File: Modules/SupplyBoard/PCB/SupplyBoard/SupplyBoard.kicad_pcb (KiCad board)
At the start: 2 copper layers, 20.3 x 8.4 mm, 4 parts, among them J1 CI_BATT, J2 USB_B_Mini, J3 Bus_PCI_Express_x1, U1 STM32L031G6Ux

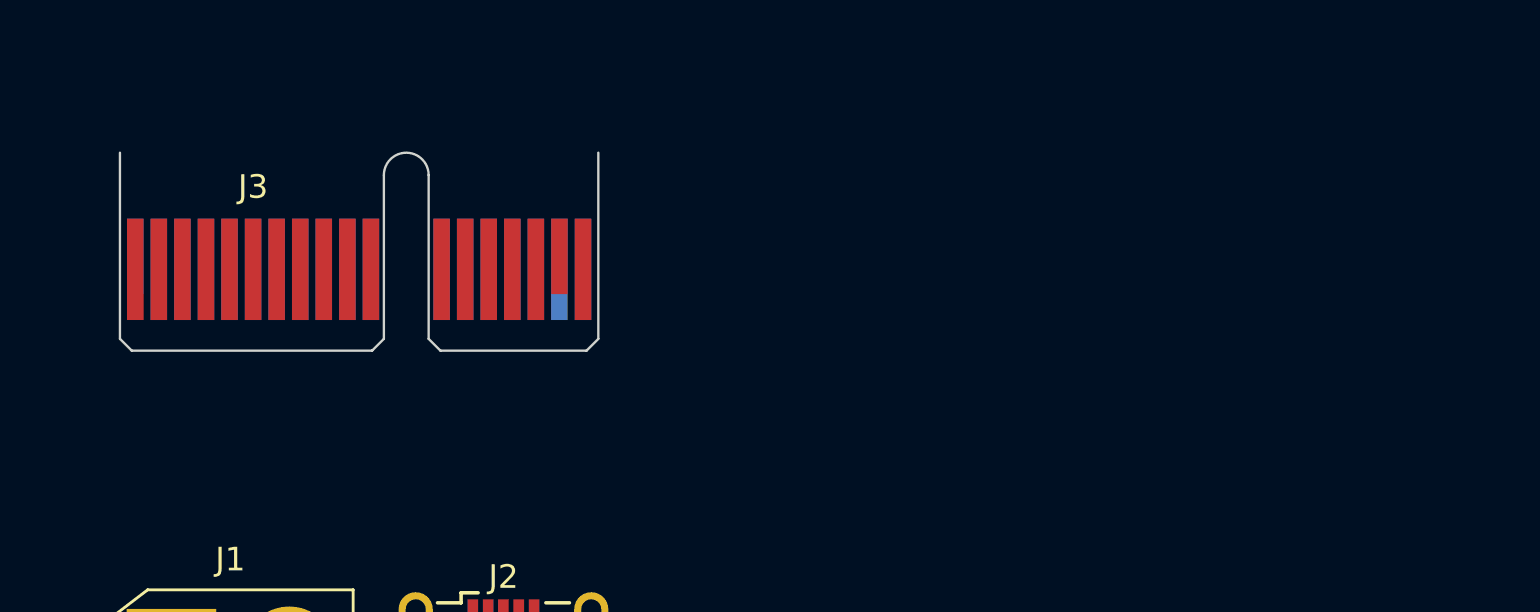
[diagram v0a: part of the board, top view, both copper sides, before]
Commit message: Lipo to 3v3 circuit added
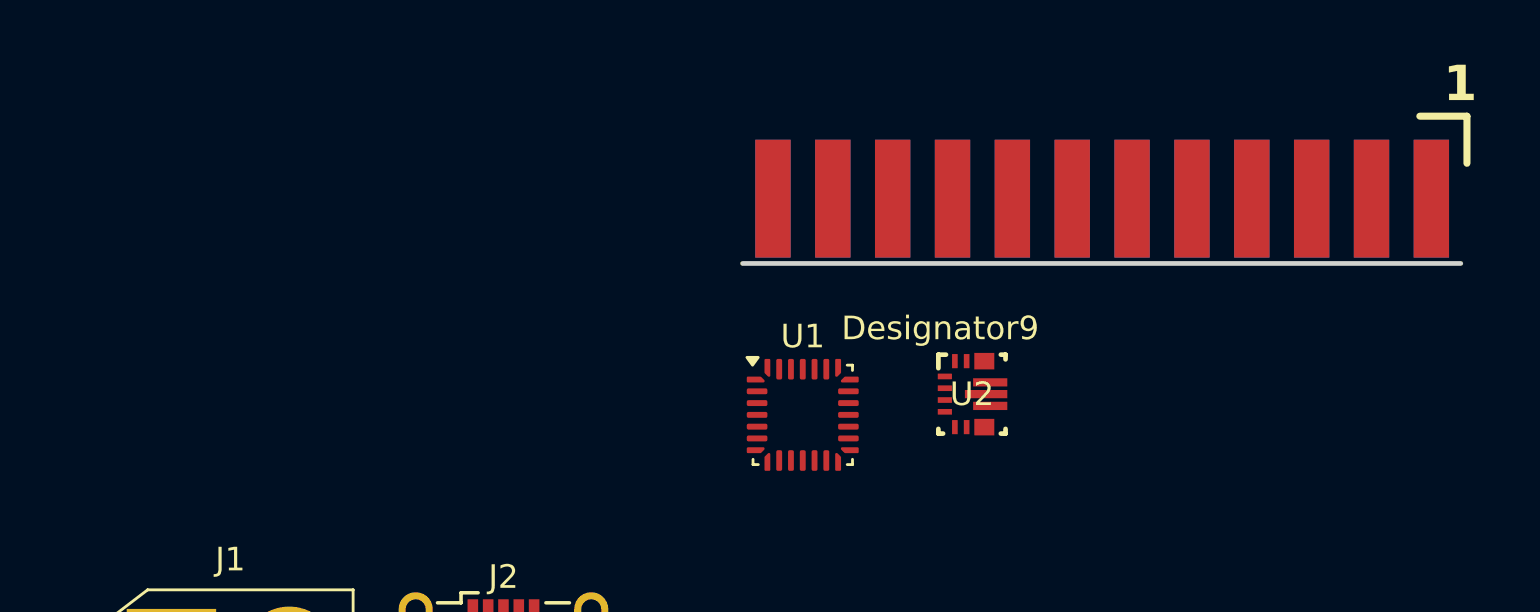
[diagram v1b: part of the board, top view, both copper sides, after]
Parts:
- added U1: STM32L031G6Ux, Package_DFN_QFN:QFN-28_4x4mm_P0.5mm, F.Cu at (104.3, 59.7)
- added U2: TPS63070, IcaroFootprints:RNM0015A, F.Cu at (111.5, 58.8)
- J3: value Bus_PCI_Express_x1 -> CIO_MAIN_CONNECTOR; footprint Connector_PCBEdge:BUS_PCIexpress_x1 -> IcaroFootprints:Connector_Icaro_Edge_tarjeta
- moved J3 41.1 mm to (117.0, 50.5)
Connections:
- J1 pad 1: unconnected-(J1-Pin_1-Pad1) -> GND
- J1 pad 2: unconnected-(J1-Pin_2-Pad2) -> /LIPO_INPUT
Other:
- board outline removed

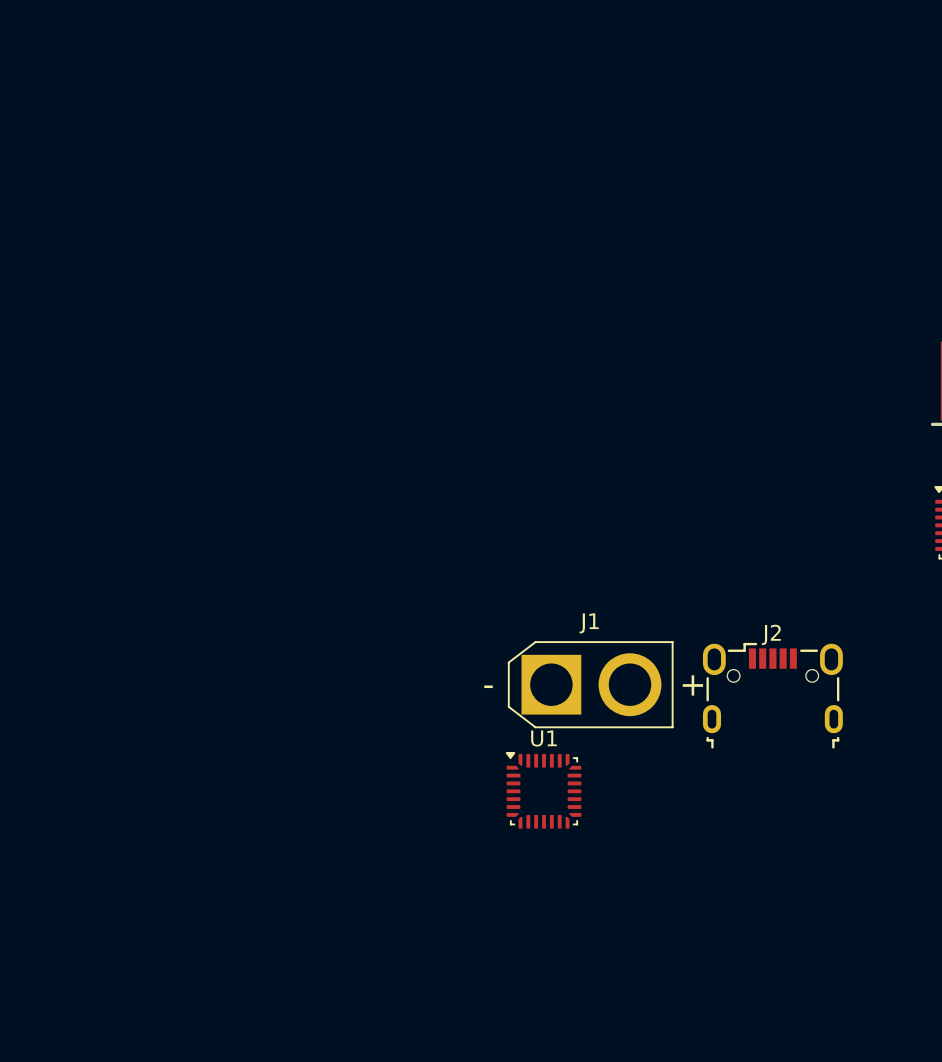
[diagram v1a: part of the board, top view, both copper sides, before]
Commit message: Added current sensor
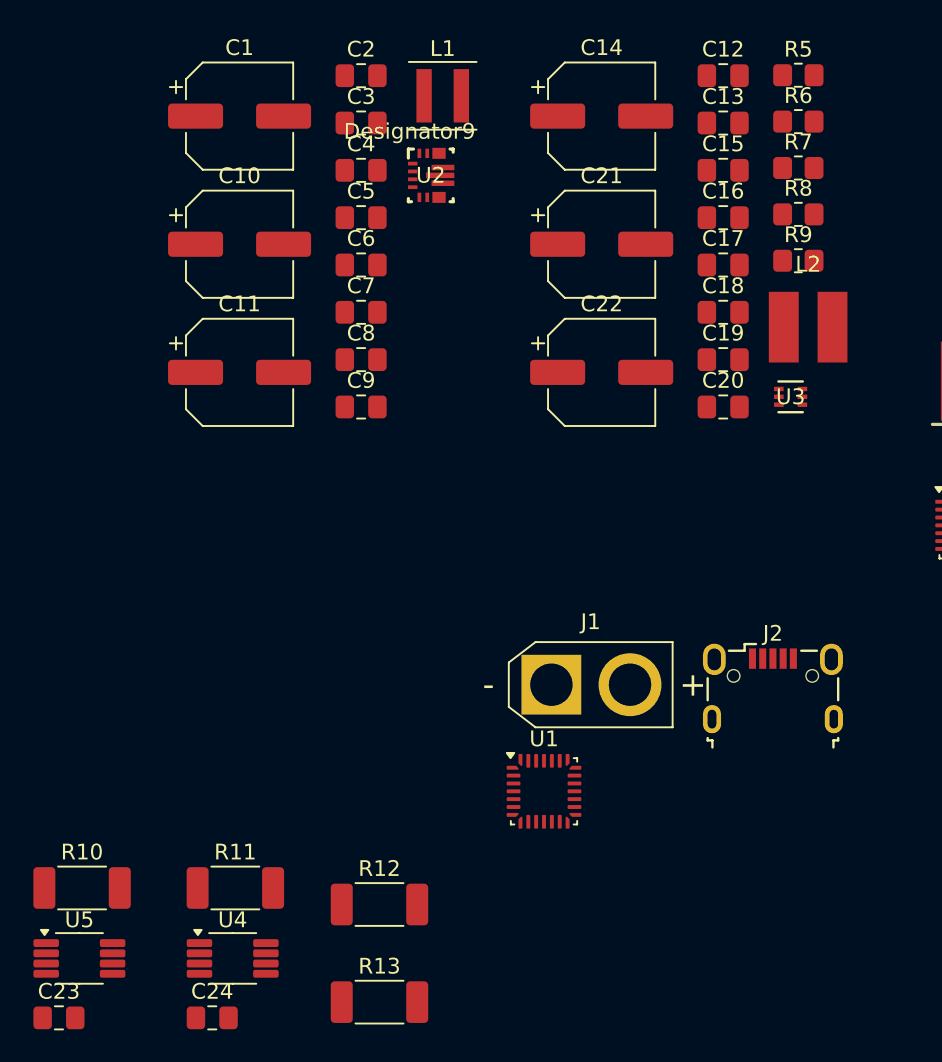
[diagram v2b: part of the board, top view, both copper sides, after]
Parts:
- added C1: 220u, Capacitor_SMD:CP_Elec_6.3x5.4, F.Cu at (57.7, 33.6)
- added C10: 220u, Capacitor_SMD:CP_Elec_6.3x5.4, F.Cu at (57.7, 41.8)
- added C11: 220u, Capacitor_SMD:CP_Elec_6.3x5.4, F.Cu at (57.7, 49.9)
- added C12: 10u, Capacitor_SMD:C_0805_2012Metric_Pad1.18x1.45mm_HandSolder, F.Cu at (88.5, 31.1)
- added C13: 10u, Capacitor_SMD:C_0805_2012Metric_Pad1.18x1.45mm_HandSolder, F.Cu at (88.5, 34.1)
- added C14: 220u, Capacitor_SMD:CP_Elec_6.3x5.4, F.Cu at (80.7, 33.6)
- added C15: 100n, Capacitor_SMD:C_0805_2012Metric_Pad1.18x1.45mm_HandSolder, F.Cu at (88.5, 37.1)
- added C16: 30p, Capacitor_SMD:C_0805_2012Metric_Pad1.18x1.45mm_HandSolder, F.Cu at (88.5, 40.1)
- added C17: 22u, Capacitor_SMD:C_0805_2012Metric_Pad1.18x1.45mm_HandSolder, F.Cu at (88.5, 43.1)
- added C18: 22u, Capacitor_SMD:C_0805_2012Metric_Pad1.18x1.45mm_HandSolder, F.Cu at (88.5, 46.1)
- added C19: 22u, Capacitor_SMD:C_0805_2012Metric_Pad1.18x1.45mm_HandSolder, F.Cu at (88.5, 49.1)
- added C2: 10u, Capacitor_SMD:C_0805_2012Metric_Pad1.18x1.45mm_HandSolder, F.Cu at (65.4, 31.1)
- added C20: 22u, Capacitor_SMD:C_0805_2012Metric_Pad1.18x1.45mm_HandSolder, F.Cu at (88.5, 52.1)
- added C21: 220u, Capacitor_SMD:CP_Elec_6.3x5.4, F.Cu at (80.7, 41.8)
- added C22: 220u, Capacitor_SMD:CP_Elec_6.3x5.4, F.Cu at (80.7, 49.9)
- added C23: 100n, Capacitor_SMD:C_0805_2012Metric_Pad1.18x1.45mm_HandSolder, F.Cu at (46.2, 91.0)
- added C24: 100n, Capacitor_SMD:C_0805_2012Metric_Pad1.18x1.45mm_HandSolder, F.Cu at (56.0, 91.0)
- added C3: 10u, Capacitor_SMD:C_0805_2012Metric_Pad1.18x1.45mm_HandSolder, F.Cu at (65.4, 34.1)
- added C4: 10n, Capacitor_SMD:C_0805_2012Metric_Pad1.18x1.45mm_HandSolder, F.Cu at (65.4, 37.1)
- added C5: 10u, Capacitor_SMD:C_0805_2012Metric_Pad1.18x1.45mm_HandSolder, F.Cu at (65.4, 40.1)
- added C6: 22u, Capacitor_SMD:C_0805_2012Metric_Pad1.18x1.45mm_HandSolder, F.Cu at (65.4, 43.1)
- added C7: 22u, Capacitor_SMD:C_0805_2012Metric_Pad1.18x1.45mm_HandSolder, F.Cu at (65.4, 46.1)
- added C8: 22u, Capacitor_SMD:C_0805_2012Metric_Pad1.18x1.45mm_HandSolder, F.Cu at (65.4, 49.1)
- added C9: 22u, Capacitor_SMD:C_0805_2012Metric_Pad1.18x1.45mm_HandSolder, F.Cu at (65.4, 52.1)
- added L1: 1.5u, Inductor_SMD:L_Coilcraft_XxL4040, F.Cu at (70.6, 32.4)
- added L2: 3.3u, IcaroFootprints:PSPCA_D43_Series, F.Cu at (93.9, 47.1)
- added R10: 50, Resistor_SMD:R_2010_5025Metric_Pad1.40x2.65mm_HandSolder, F.Cu at (47.7, 82.7)
- added R11: 50, Resistor_SMD:R_2010_5025Metric_Pad1.40x2.65mm_HandSolder, F.Cu at (57.4, 82.7)
- added R12: 50, Resistor_SMD:R_2010_5025Metric_Pad1.40x2.65mm_HandSolder, F.Cu at (66.6, 83.8)
- added R13: 50, Resistor_SMD:R_2010_5025Metric_Pad1.40x2.65mm_HandSolder, F.Cu at (66.6, 90.0)
- added R5: 10k, Resistor_SMD:R_0805_2012Metric_Pad1.20x1.40mm_HandSolder, F.Cu at (93.2, 31.0)
- added R6: 22k, Resistor_SMD:R_0805_2012Metric_Pad1.20x1.40mm_HandSolder, F.Cu at (93.2, 34.0)
- added R7: 22k, Resistor_SMD:R_0805_2012Metric_Pad1.20x1.40mm_HandSolder, F.Cu at (93.2, 36.9)
- added R8: 22k, Resistor_SMD:R_0805_2012Metric_Pad1.20x1.40mm_HandSolder, F.Cu at (93.2, 39.9)
- added R9: 22k, Resistor_SMD:R_0805_2012Metric_Pad1.20x1.40mm_HandSolder, F.Cu at (93.2, 42.8)
- added U2: TPS63070, IcaroFootprints:RNM0015A, F.Cu at (69.9, 37.4)
- added U3: ~, IcaroFootprints:TPS564242DRLR_TEX, F.Cu at (92.8, 51.5)
- added U4: ~, Package_SO:VSSOP-8_3x3mm_P0.65mm, F.Cu at (57.3, 87.2)
- added U5: ~, Package_SO:VSSOP-8_3x3mm_P0.65mm, F.Cu at (47.5, 87.2)
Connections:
- J1 pad 2: /LIPO_INPUT -> /CurrentSense_Lipo/V_IN_{1}

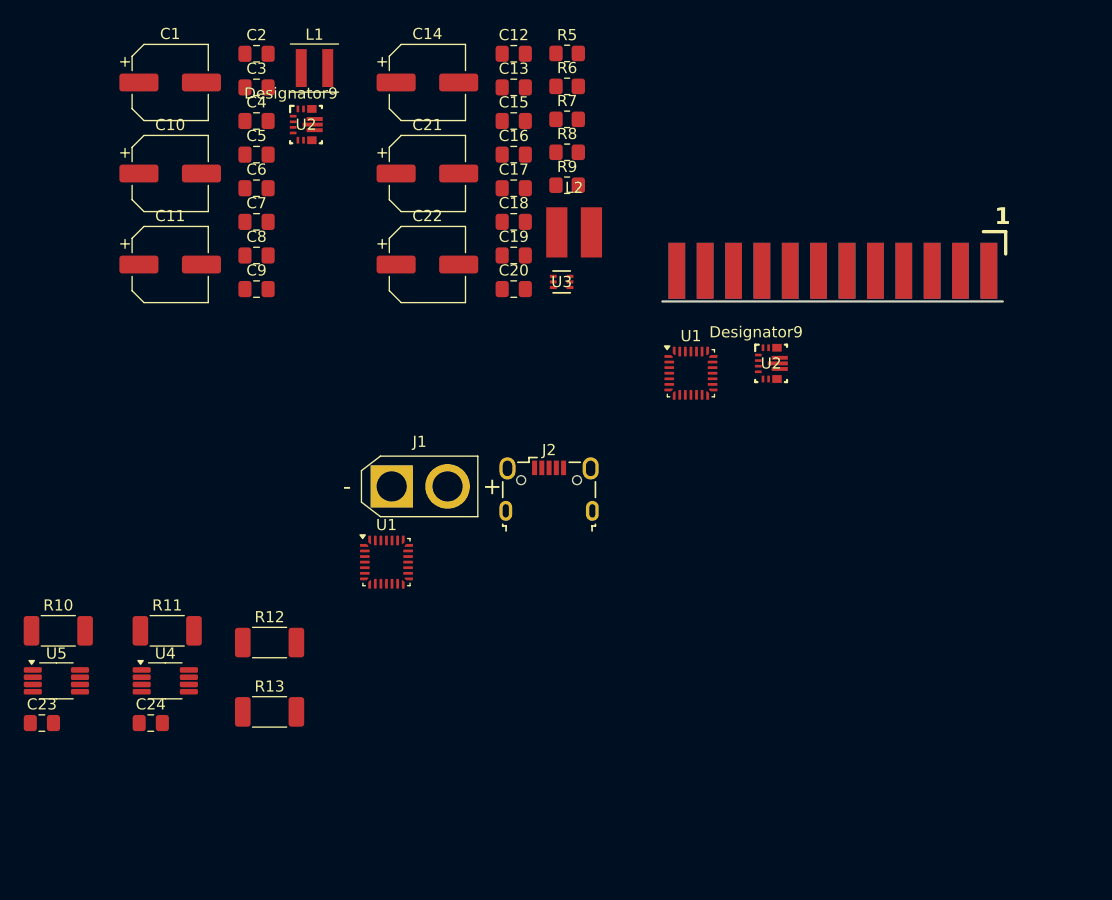
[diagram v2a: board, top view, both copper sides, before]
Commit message: Supply board schematic and PCB
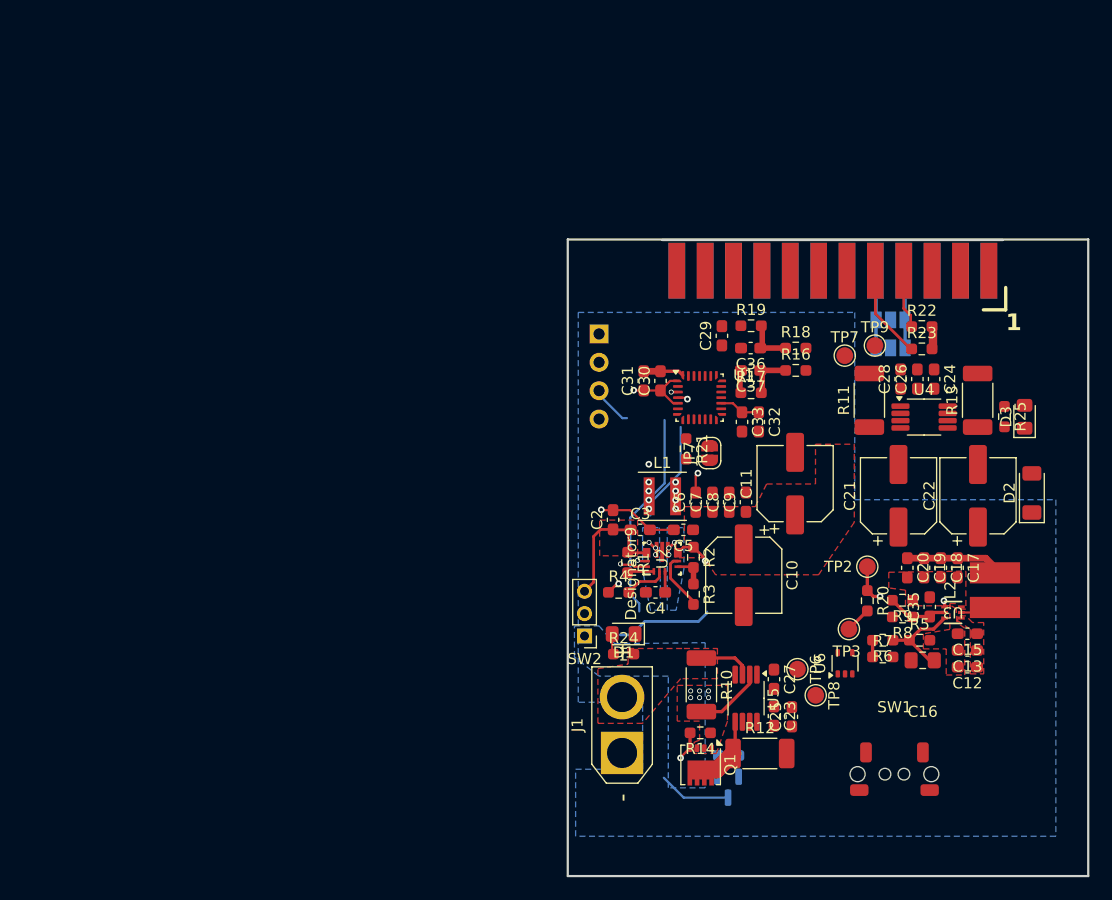
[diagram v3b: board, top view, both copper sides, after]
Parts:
- removed C1, C14: 220u, Capacitor_SMD:CP_Elec_6.3x5.4
- removed the U1 at (104.3, 59.7)
- removed the U2 at (111.5, 58.8)
- added C25: 100n, Capacitor_SMD:C_0603_1608Metric_Pad1.08x0.95mm_HandSolder, F.Cu at (113.4, 90.4)
- added C26: 100n, Capacitor_SMD:C_0603_1608Metric_Pad1.08x0.95mm_HandSolder, F.Cu at (124.6, 60.2)
- added C27: 100n, Capacitor_SMD:C_0603_1608Metric_Pad1.08x0.95mm_HandSolder, F.Cu at (111.8, 87.1)
- added C28: 100n, Capacitor_SMD:C_0603_1608Metric_Pad1.08x0.95mm_HandSolder, F.Cu at (123.1, 60.2)
- added C29: 0.1u, Capacitor_SMD:C_0603_1608Metric_Pad1.08x0.95mm_HandSolder, F.Cu at (107.1, 56.3)
- added C30: 10u, Capacitor_SMD:C_0603_1608Metric_Pad1.08x0.95mm_HandSolder, F.Cu at (101.6, 60.4)
- added C31: 22n, Capacitor_SMD:C_0603_1608Metric_Pad1.08x0.95mm_HandSolder, F.Cu at (100.1, 60.4)
- added C32: 10u, Capacitor_SMD:C_0603_1608Metric_Pad1.08x0.95mm_HandSolder, F.Cu at (110.4, 64.0)
- added C33: 22n, Capacitor_SMD:C_0603_1608Metric_Pad1.08x0.95mm_HandSolder, F.Cu at (108.9, 64.0)
- added C35: 100n, Capacitor_SMD:C_0603_1608Metric_Pad1.08x0.95mm_HandSolder, F.Cu at (125.7, 80.6)
- added C36: 0.1u, Capacitor_SMD:C_0603_1608Metric_Pad1.08x0.95mm_HandSolder, F.Cu at (109.7, 57.4)
- added C37: 0.1u, Capacitor_SMD:C_0603_1608Metric_Pad1.08x0.95mm_HandSolder, F.Cu at (109.7, 59.4)
- added D1: LED, LED_SMD:LED_0805_2012Metric_Pad1.15x1.40mm_HandSolder, F.Cu at (98.3, 83.0)
- added D2: ZMM3v3, Diode_SMD:D_MiniMELF, F.Cu at (134.9, 70.4)
- added D3: LED, LED_SMD:LED_0805_2012Metric_Pad1.15x1.40mm_HandSolder, F.Cu at (134.2, 63.6)
- added JP5: TX, Jumper:SolderJumper-3_P1.3mm_Open_Pad1.0x1.5mm, B.Cu at (122.2, 54.9)
- added JP6: RX, Jumper:SolderJumper-3_P1.3mm_Open_Pad1.0x1.5mm, B.Cu at (122.2, 57.4)
- added JP7: boot_jumper, Jumper:SolderJumper-2_P1.3mm_Open_RoundedPad1.0x1.5mm, F.Cu at (106.0, 66.8)
- added Q1: AGP30P35AP, Package_SON:Diodes_PowerDI3333-8, F.Cu at (105.2, 94.7)
- added Q2: IRLM2502, Package_TO_SOT_SMD:SOT-23, B.Cu at (107.7, 96.7)
- added R1: 10k, Resistor_SMD:R_0603_1608Metric_Pad0.98x0.95mm_HandSolder, F.Cu at (98.7, 76.6)
- added R14: 1Meg, Resistor_SMD:R_0603_1608Metric_Pad0.98x0.95mm_HandSolder, F.Cu at (105.2, 91.9)
- added R15: 1Meg, Resistor_SMD:R_0603_1608Metric_Pad0.98x0.95mm_HandSolder, B.Cu at (107.7, 93.9)
- added R16: R_Small, Resistor_SMD:R_0603_1608Metric_Pad0.98x0.95mm_HandSolder, F.Cu at (113.7, 59.4)
- added R17: 10k, Resistor_SMD:R_0603_1608Metric_Pad0.98x0.95mm_HandSolder, F.Cu at (109.7, 61.4)
- added R18: 10k, Resistor_SMD:R_0603_1608Metric_Pad0.98x0.95mm_HandSolder, F.Cu at (113.7, 57.4)
- added R19: 10k, Resistor_SMD:R_0603_1608Metric_Pad0.98x0.95mm_HandSolder, F.Cu at (109.7, 55.4)
- added R2: 680k, Resistor_SMD:R_0603_1608Metric_Pad0.98x0.95mm_HandSolder, F.Cu at (104.6, 76.2)
- added R20: 10k, Resistor_SMD:R_0603_1608Metric_Pad0.98x0.95mm_HandSolder, F.Cu at (120.1, 80.0)
- added R21: 10k, Resistor_SMD:R_0603_1608Metric_Pad0.98x0.95mm_HandSolder, F.Cu at (103.9, 66.5)
- added R22: 2k2, Resistor_SMD:R_0603_1608Metric_Pad0.98x0.95mm_HandSolder, F.Cu at (125.0, 55.5)
- added R23: 2k2, Resistor_SMD:R_0603_1608Metric_Pad0.98x0.95mm_HandSolder, F.Cu at (125.0, 57.5)
- added R24: 2k2, Resistor_SMD:R_0603_1608Metric_Pad0.98x0.95mm_HandSolder, F.Cu at (98.3, 84.8)
- added R25: 2k2, Resistor_SMD:R_0603_1608Metric_Pad0.98x0.95mm_HandSolder, F.Cu at (132.4, 63.6)
- added R3: 130k, Resistor_SMD:R_0603_1608Metric_Pad0.98x0.95mm_HandSolder, F.Cu at (104.6, 79.5)
- added R4: 100k, Resistor_SMD:R_0603_1608Metric_Pad0.98x0.95mm_HandSolder, F.Cu at (97.9, 79.3)
- added SW1: RESET, IcaroFootprints:SideSwitch_2.7_4.65, F.Cu at (122.5, 95.6)
- added SW2: SW_SPDT_312, Connector_PinHeader_2.00mm:PinHeader_1x03_P2.00mm_Vertical, F.Cu at (94.8, 83.2)
- added TP2: 3v3_PG, TestPoint:TestPoint_Pad_D1.5mm, F.Cu at (120.1, 77.0)
- added TP3: 3v3_PG_VCC, TestPoint:TestPoint_Pad_D1.5mm, F.Cu at (118.5, 82.6)
- added TP6: I1, TestPoint:TestPoint_Pad_D1.5mm, F.Cu at (113.9, 86.2)
- added TP7: I1, TestPoint:TestPoint_Pad_D1.5mm, F.Cu at (118.1, 58.1)
- added TP8: I2, TestPoint:TestPoint_Pad_D1.5mm, F.Cu at (115.5, 88.5)
- added TP9: I2, TestPoint:TestPoint_Pad_D1.5mm, F.Cu at (120.8, 57.2)
- added U6: TMP20AIDCK, Package_TO_SOT_SMD:SOT-353_SC-70-5, F.Cu at (118.1, 85.6)
- C12, C13, C15, C17, C18, C19, C2, C20, C23, C24, C3, C4, C5, C6, C7, C8, C9: footprint Capacitor_SMD:C_0805_2012Metric_Pad1.18x1.45mm_HandSolder -> Capacitor_SMD:C_0603_1608Metric_Pad1.08x0.95mm_HandSolder
- J2: value USB_B_Mini -> SW-DP; footprint Connector_USB:USB_Micro-B_Wuerth_629105150521 -> Connector_PinHeader_2.54mm:PinHeader_1x04_P2.54mm_Vertical; moved to B.Cu
- R5, R6, R7, R8, R9: footprint Resistor_SMD:R_0805_2012Metric_Pad1.20x1.40mm_HandSolder -> Resistor_SMD:R_0603_1608Metric_Pad0.98x0.95mm_HandSolder
- moved C24 76.6 mm to (126.1, 60.2), turned to -90 degrees
- moved U4 71.9 mm to (125.2, 63.6)
- moved R13 69.3 mm to (130.0, 62.1), turned to 90 degrees
- moved C12 68.3 mm to (129.1, 86.0), turned to 180 degrees
- moved R11 66.2 mm to (120.3, 62.1), turned to 90 degrees
- moved C23 65.6 mm to (111.8, 90.4), turned to -90 degrees
- moved C13 64.7 mm to (129.1, 84.5), turned to 180 degrees
- moved C10 62.7 mm to (109.1, 77.8), turned to -90 degrees
- moved U5 61.8 mm to (109.3, 88.8), turned to -90 degrees
- moved C15 61.3 mm to (129.1, 83.0), turned to 180 degrees
- moved R5 61.3 mm to (124.8, 83.6)
- moved C11 59.3 mm to (113.7, 69.6), turned to 90 degrees
- moved C16 58.2 mm to (125.1, 85.4), turned to 180 degrees
- moved R10 57.8 mm to (105.3, 87.6), turned to -90 degrees
- moved R6 57.1 mm to (121.5, 83.6), turned to 180 degrees
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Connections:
- net /CurrentSense_regulated/V_IN_{1} renamed /LIPO_TO_5V/5V_OUT
- net /CurrentSense_regulated/V_IN_{2} renamed /LIPO_TO_3V/3V3_OUT
- net Net-(U2-VAUX) renamed /LIPO_TO_5V/AUX
- C12 pad 1: /BATT_INPUT -> /Controlador/BATT_INPUT
- C13 pad 1: /BATT_INPUT -> /Controlador/BATT_INPUT
- C15 pad 1: /BATT_INPUT -> /Controlador/BATT_INPUT
- C2 pad 1: /BATT_INPUT -> /Controlador/BATT_INPUT
- C3 pad 1: /BATT_INPUT -> /Controlador/BATT_INPUT
- J2 pad 1: unconnected-(J2-VBUS-Pad1) -> +3.3V
- J2 pad 2: unconnected-(J2-D--Pad2) -> /Controlador/SWDIO
- J2 pad 3: unconnected-(J2-D+-Pad3) -> /Controlador/SWCLK
- J2 pad 4: unconnected-(J2-ID-Pad4) -> GND
- J3 pad 10: unconnected-(J3-UART_RX-Pad10) -> /C_UART_RX
- J3 pad 18: unconnected-(J3-MOSI-Pad18) -> /SPI.MOSI
- J3 pad 20: unconnected-(J3-MISO-Pad20) -> /SPI.MISO
- J3 pad 21: unconnected-(J3-CS0-Pad21) -> GND
- J3 pad 22: unconnected-(J3-CS1-Pad22) -> /SPI.SCK
- J3 pad 23: unconnected-(J3-CS2-Pad23) -> /SPI.CS1
- J3 pad 24: unconnected-(J3-CS3-Pad24) -> /SPI.CS0
- J3 pad 8: unconnected-(J3-UART_TX-Pad8) -> /C_UART_TX
- J3 pad 9: /I2C0_SDA -> /I2C0_SCL
- R8 pad 2: /BATT_INPUT -> /Controlador/BATT_INPUT
- U1 pad 1: unconnected-(U1-VDD-Pad1) -> +3.3V
- U1 pad 10: unconnected-(U1-PA4-Pad10) -> /I_{IN}_SENSE
- U1 pad 11: unconnected-(U1-PA5-Pad11) -> /I_{BYPASS}_SENSE
- U1 pad 12: unconnected-(U1-PA6-Pad12) -> /Controlador/TEMP_SENSOR
- U1 pad 13: unconnected-(U1-PA7-Pad13) -> /SPI.CS0
- U1 pad 14: unconnected-(U1-PB0-Pad14) -> /SPI.MOSI
- U1 pad 15: unconnected-(U1-PB1-Pad15) -> /SPI.MISO
- U1 pad 16: Net-(U1-VSS-Pad16) -> GND
- U1 pad 17: unconnected-(U1-VDD-Pad17) -> +3.3V
- U1 pad 18: unconnected-(U1-PA8-Pad18) -> /SPI.CS1
- U1 pad 19: unconnected-(U1-PA9-Pad19) -> /I2C0_SCL
- U1 pad 2: unconnected-(U1-PC14-Pad2) -> /BYPASS_EN
- U1 pad 20: unconnected-(U1-PA10-Pad20) -> /I2C0_SDA
- U1 pad 21: unconnected-(U1-PA13-Pad21) -> /Controlador/SWDIO
- U1 pad 22: unconnected-(U1-PA14-Pad22) -> /Controlador/SWCLK
- U1 pad 23: unconnected-(U1-PA15-Pad23) -> Net-(U1-PA15)
- U1 pad 24: unconnected-(U1-PB3-Pad24) -> /SPI.SCK
- U1 pad 25: unconnected-(U1-PB6-Pad25) -> /Controlador/UART_TX
- U1 pad 26: unconnected-(U1-PB7-Pad26) -> /Controlador/UART_RX
- U1 pad 27: unconnected-(U1-BOOT0-Pad27) -> Net-(JP7-B)
- U1 pad 28: Net-(U1-VSS-Pad16) -> GND
- U1 pad 3: unconnected-(U1-PC15-Pad3) -> /Controlador/5V_ENABLE
- U1 pad 4: unconnected-(U1-NRST-Pad4) -> /Controlador/~{RESET}
- U1 pad 5: unconnected-(U1-VDDA-Pad5) -> +3.3V
- U1 pad 6: unconnected-(U1-PA0-Pad6) -> /Controlador/V_{IN}_SENSE
- U1 pad 7: unconnected-(U1-PA1-Pad7) -> /Controlador/V_{5V}_SENSE
- U1 pad 8: unconnected-(U1-PA2-Pad8) -> /I_{3v3}_SENSE
- U1 pad 9: unconnected-(U1-PA3-Pad9) -> /I_{5v}_SENSE
- U2 pad 12: /BATT_INPUT -> /Controlador/BATT_INPUT
- U2 pad 13: /BATT_INPUT -> /Controlador/BATT_INPUT
- U2 pad 5: Net-(U2-FB) -> /LIPO_TO_5V/FB
- U3 pad 1: /BATT_INPUT -> /Controlador/BATT_INPUT
- U3 pad 4: unconnected-(U3-PG-Pad4) -> Net-(U3-PG)
- U4 pad 1: /CurrentSense_regulated/V_SENSE_{1} -> /I_{5v}_SENSE
- U4 pad 7: /CurrentSense_regulated/V_SENSE_{2} -> /I_{3v3}_SENSE
- U5 pad 1: /CurrentSense_Lipo/V_SENSE_{1} -> /I_{IN}_SENSE
- U5 pad 7: /CurrentSense_Lipo/V_SENSE_{2} -> /I_{BYPASS}_SENSE
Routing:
- net GND: track 0.00 -> 22.1 mm, vias 0 -> 3
- net /Controlador/5V_ENABLE: track 0.00 -> 20.2 mm, vias 0 -> 2
- net /LIPO_TO_5V/5V_OUT: track 0.00 -> 13.2 mm, vias 0 -> 2
- net /Controlador/BATT_INPUT: track 0.00 -> 12.4 mm
- net +3.3V: track 0.00 -> 12.0 mm, vias 0 -> 1
- net /Controlador/~{RESET}: track 0.00 -> 9.93 mm, vias 0 -> 2
- net Net-(Q1-G): track 0.00 -> 9.09 mm, vias 0 -> 1
- net /LIPO_TO_3V/3V3_OUT: track 0.00 -> 8.44 mm
- net Net-(U3-FB): track 0.00 -> 8.42 mm
- net /I2C0_SCL: track 0.00 -> 8.31 mm
- net /C_UART_TX: track 0.00 -> 6.95 mm
- net /C_UART_RX: track 0.00 -> 6.92 mm
- net /BATT_BYPASS_SW/BATT_OUT: track 0.00 -> 6.43 mm
- net /BATT_INPUT: track 0.00 -> 6.17 mm, vias 0 -> 6
- net Net-(U3-EN): track 0.00 -> 5.47 mm
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- added copper zone on B.Cu, net /BATT_INPUT
- added copper zone on F.Cu, net /BATT_INPUT
- added copper zone on F.Cu, net /CurrentSense_Lipo/V_IN_{1}
- added copper zone on F.Cu, net /LIPO_TO_5V/5V_OUT
- added copper zone on B.Cu, net GND
- added copper zone on F.Cu, net GND
- added copper zone on B.Cu, net Net-(L1-+)
- added copper zone on B.Cu, net Net-(L1--)
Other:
- board outline added: 46.6 x 57 mm
